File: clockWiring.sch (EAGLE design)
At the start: 8 parts

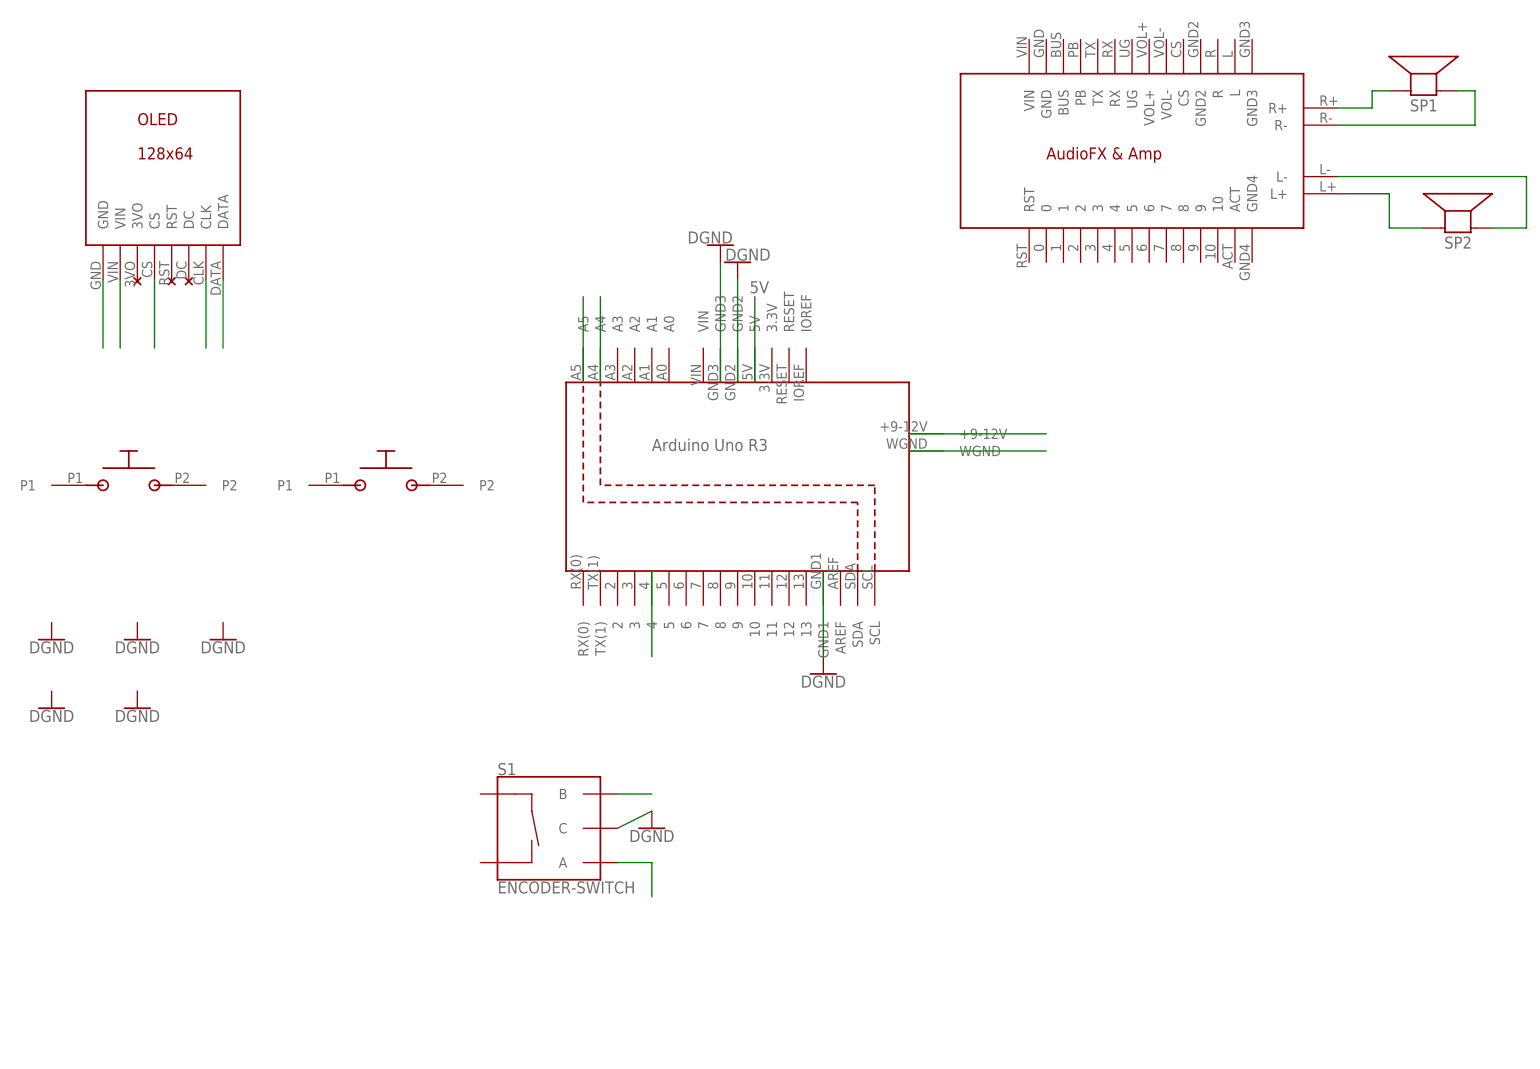
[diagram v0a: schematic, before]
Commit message: add wiring connections to schematic.
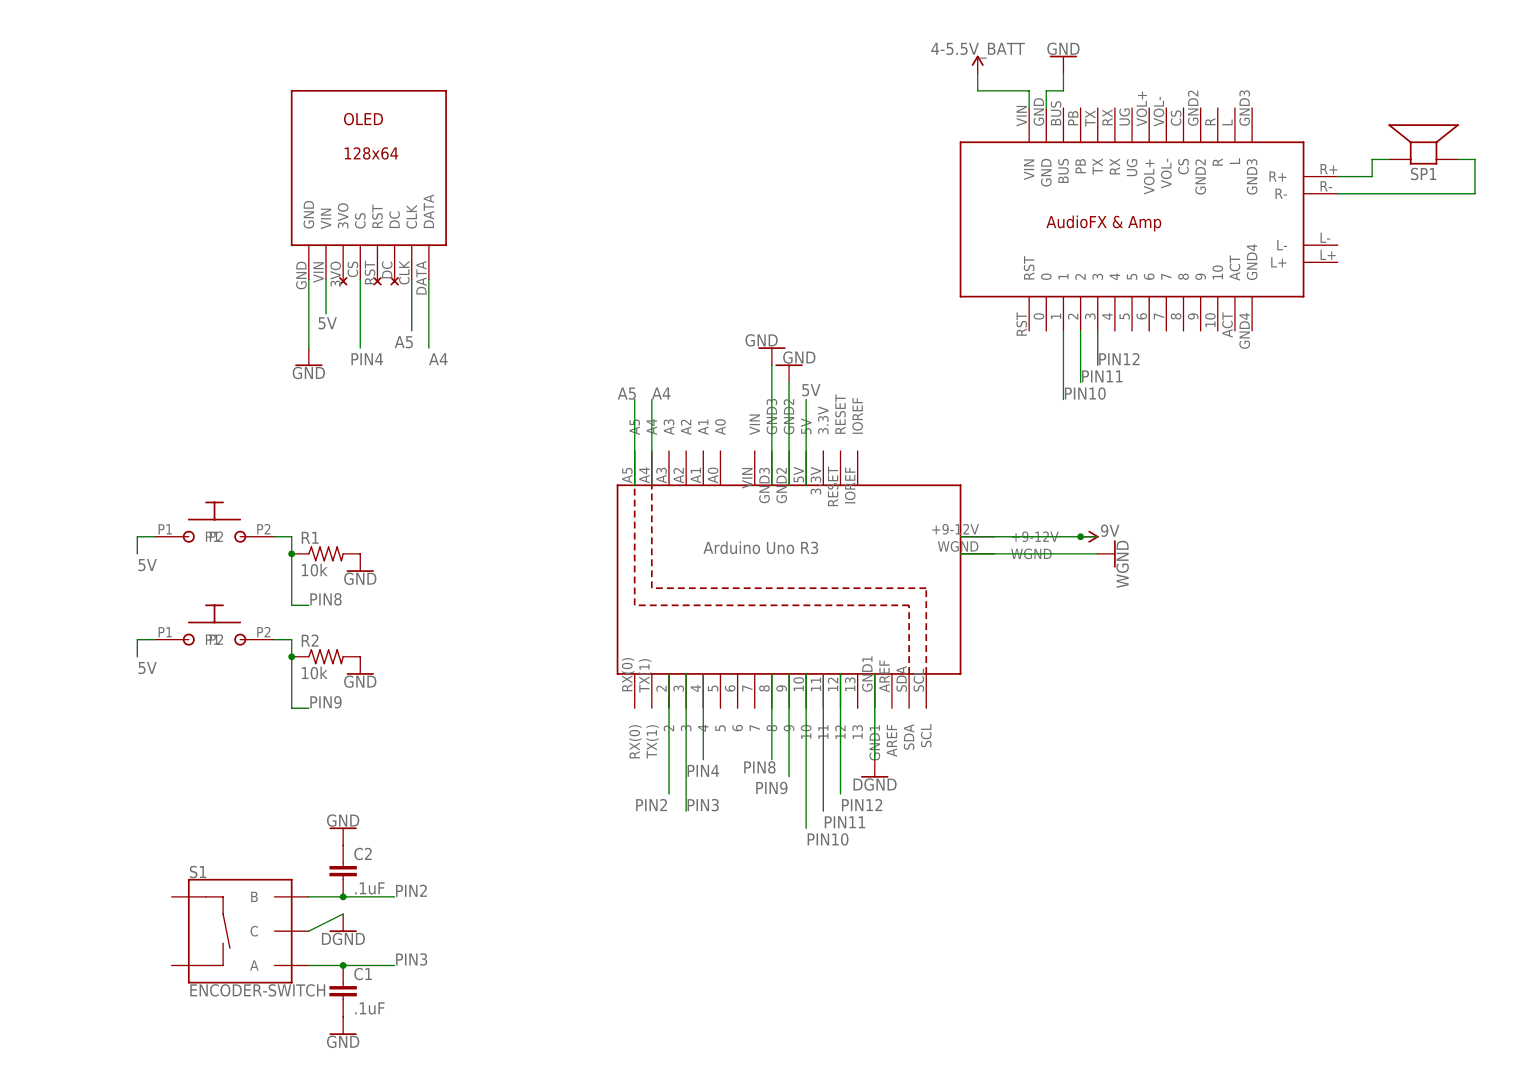
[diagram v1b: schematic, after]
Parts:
- removed SP2: SPEAKER/PS12, adafruit:SPEAKER/PS12
- added C1, C2: .1uF, capacitor-wima:C2.5/2
- added R1, R2: 10k, adafruit:FLIPFLOP-RES
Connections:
- net N$16 renamed 12V
- removed net N$1: SP2.+, U$5.L+
- removed net N$10: U$6.A5
- removed net N$11: U$6.A4
- removed net N$12: U$6.4
- removed net N$13: S1.A
- removed net N$14: S1.B
- removed net N$17: U$6.WGND
- removed net N$2: SP2.-, U$5.L-
- removed net N$5: U$2.CLK
- removed net N$6: U$2.DATA
- removed net N$7: U$2.CS
- removed net N$8: U$2.GND
- removed net N$9: U$2.VIN
- new net A4: U$2.DATA, U$6.A4
- new net A5: U$2.CLK, U$6.A5
- new net PIN10: U$5.1, U$6.10
- new net PIN11: U$5.2, U$6.11
- new net PIN12: U$5.3, U$6.12
- new net PIN2: C2.2, S1.B, U$6.2
- new net PIN3: C1.1, S1.A, U$6.3
- new net PIN4: U$2.CS, U$6.4
- new net PIN8: R1.1, U$6.8, U$7.P2
- new net PIN9: R2.1, U$6.9, U$8.P2
- new net V_BATT: U$5.VIN
- net 5V: now also U$2.VIN, U$7.P1, U$8.P1
- net GND: now also C1.2, C2.1, R1.2, R2.2, U$2.GND, U$5.GND, U$6.WGND
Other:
- moved on the sheet: S1, SP1
